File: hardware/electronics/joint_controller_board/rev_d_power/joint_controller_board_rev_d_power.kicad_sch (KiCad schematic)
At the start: 41 parts, among them J1 J_IFACE, J2 J_PWR_IN_RAW, J4 J_PWR_OUT_SW, Q1 BSC016N06NS, Q2 BSC016N06NS, U1 TPS2492PW, U2 LMR36520ADDA, U3 TLV75533PDBV

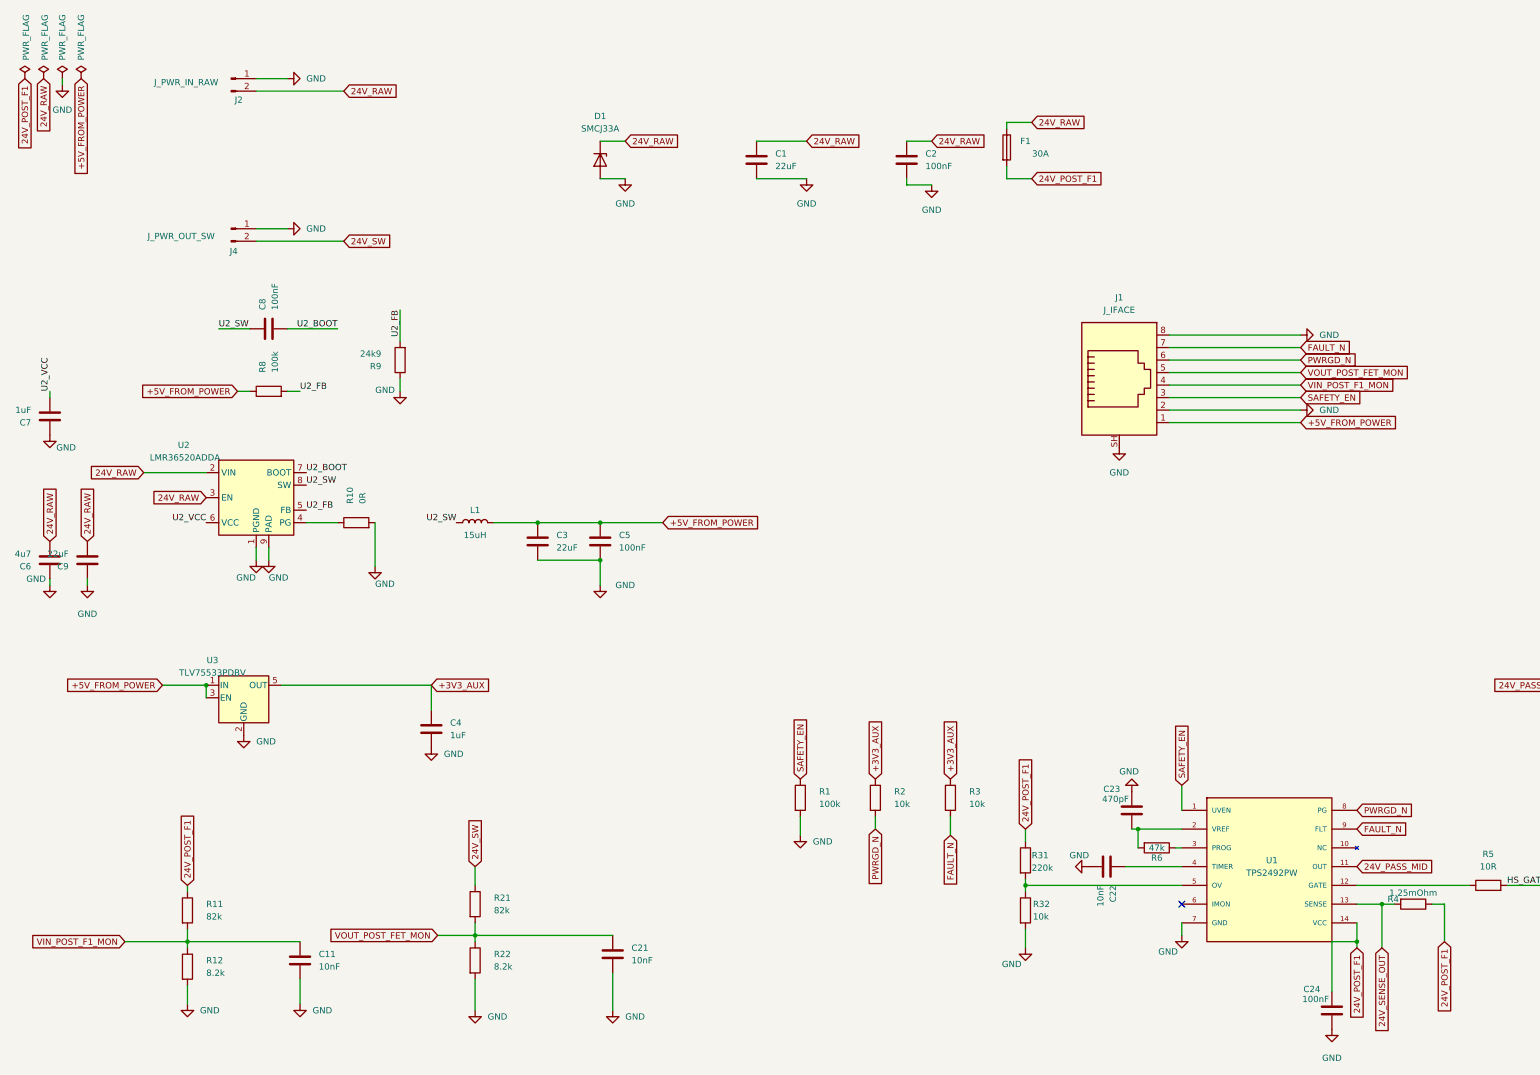
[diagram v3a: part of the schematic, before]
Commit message: feat(rev_d_power): move branch fuse off-board to upstream PDU (Option C1)
Remove on-board F1 fuse + holder from schematic and layout. Per-joint 30A ATO
slow-blow now lives on the upstream PDU / battery distribution board. Saves
~24mm vertical clearance inside joint enclosure (resolved mechanical fit-check
blocker) and protects the full cable run rather than only the PCB. On-board
fast protection preserved via TPS2492 current-limit (~40A latch-off).

Net renames: 24V_POST_F1 -> 24V_RAW (unified), VIN_POST_F1_MON -> VIN_RAW_MON.
RJ45 pin 4 signal name and related schematic descriptions updated accordingly
in ARCHITECTURE.md and COMPONENT_SELECTION.md.

ERC 0/0, DRC 0 violations (2 preexisting XT60 J2/J4 gender-swap warnings
unchanged).

Signed-off-by: graceful-kinematics <info@aliahumanoid.com>
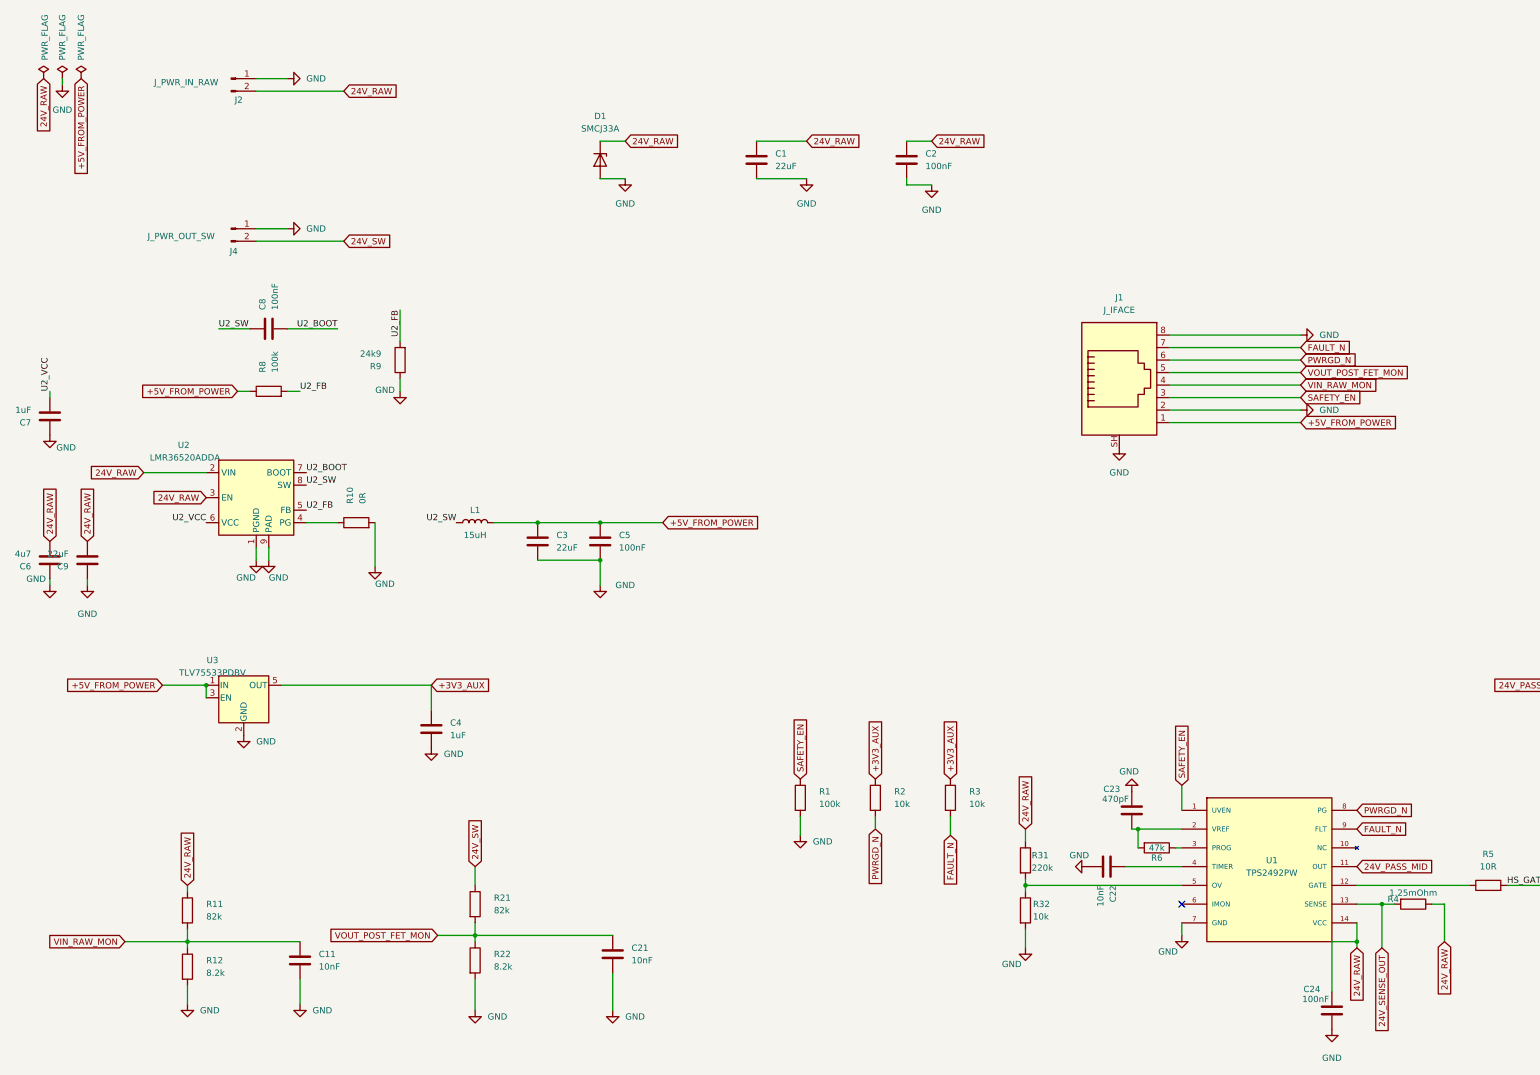
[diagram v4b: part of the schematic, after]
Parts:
- removed F1: 30A, rev_d_power_footprints:FuseHolder_Blade_ATO_Littelfuse_FLR_178.6165, symbol Device:Fuse
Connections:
- net 24V_POST_F1 is gone; now on net 24V_RAW: C24.2, R11.1, R31.1, R4.1, U1.14 (VCC)
- net VIN_POST_F1_MON renamed VIN_RAW_MON

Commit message: feat(rev_d_power): remove raw daisy-chain J3, align XT60 library prefix
Drop the J3 XT60PW-F raw-pass-through connector and its dedicated copper.
The board now has a single raw-input (J2 XT60PW-F) and a single switched
motor output (J4 XT60PW-M). Branch fan-out is handled by the upstream PDU,
consistent with Option C1 external fusing landed in the previous commit.

Also align the J2/J4 footprint library references with the matching
schematic symbols by adding the explicit Connector_AMASS: prefix. Clears
the last two footprint_symbol_mismatch DRC schematic-parity warnings.

Docs updated:
- ARCHITECTURE.md: External Interfaces lists only J_PWR_IN_RAW and
  J_PWR_OUT_SW; Architecture Decision 1 rewritten as "No on-board raw
  daisy-chain output"; power diagram, 6 "Raw daisy-chain sizing" section,
  and test-point list trimmed accordingly; IMON note: pin budget full, not
  routed to RJ45 in this revision.
- COMPONENT_SELECTION.md: topology reflects no raw daisy-chain.
- README.md: board size corrected to 40x60 mm; J2/J4 gender listed; ERC 0/0
  and DRC 0 documented.

ERC 0/0. DRC: 0 violations, 0 unconnected pads, 0 footprint errors.
Board size 40 x 60 mm. BOM 27 rows (was 28 with J3).

Signed-off-by: graceful-kinematics <info@aliahumanoid.com>
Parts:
- J2: footprint Connector_AMASS:AMASS_XT60PW-M_1x02_P7.20mm_Horizontal -> Connector_AMASS:AMASS_XT60PW-F_1x02_P7.20mm_Horizontal; MPN XT60PW-M -> XT60PW-F
- J4: footprint Connector_AMASS:AMASS_XT60PW-F_1x02_P7.20mm_Horizontal -> Connector_AMASS:AMASS_XT60PW-M_1x02_P7.20mm_Horizontal; MPN XT60PW-F -> XT60PW-M
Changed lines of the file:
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@@
 			)
 		)
-		(property "Footprint" "Connector_AMASS:AMASS_XT60PW-M_1x02_P7.20mm_Horizontal"
+		(property "Footprint" "Connector_AMASS:AMASS_XT60PW-F_1x02_P7.20mm_Horizontal"
 			(at 62.23 29.21 0)
 			(effects
@@
 			)
 		)
-		(property "Description" "Raw 24V input XT60"
+		(property "Description" "Raw 24V input XT60 female connector"
 			(at 62.23 29.21 0)
 			(effects
@@
 			)
 		)
-		(property "MPN" "XT60PW-M"
+		(property "MPN" "XT60PW-F"
 			(at 62.23 29.21 0)
 			(effects
@@
 			)
 		)
-		(property "Footprint" "Connector_AMASS:AMASS_XT60PW-F_1x02_P7.20mm_Horizontal"
+		(property "Footprint" "Connector_AMASS:AMASS_XT60PW-M_1x02_P7.20mm_Horizontal"
 			(at 62.23 59.69 0)
 			(effects
@@
 			)
 		)
-		(property "Description" "Switched 24V output XT60"
+		(property "Description" "Switched 24V output XT60 male connector"
 			(at 62.23 59.69 0)
 			(effects
@@
 			)
 		)
-		(property "MPN" "XT60PW-F"
+		(property "MPN" "XT60PW-M"
 			(at 62.23 59.69 0)
 			(effects

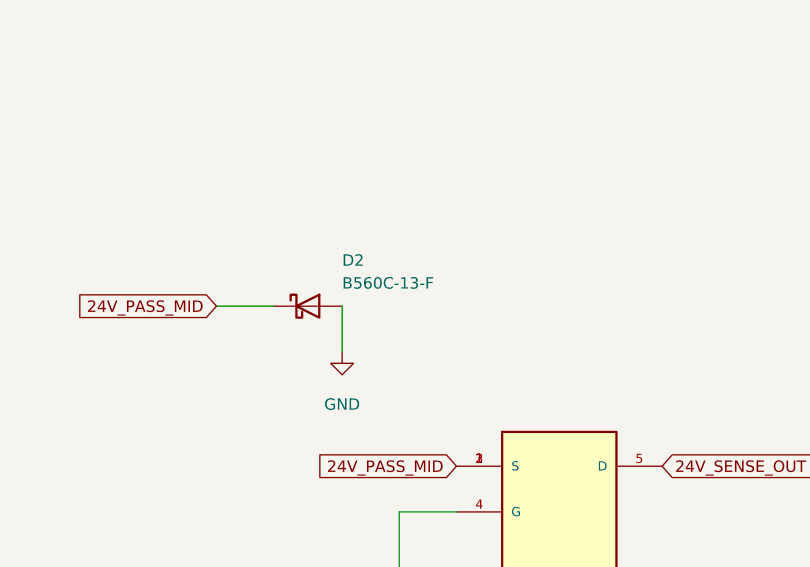
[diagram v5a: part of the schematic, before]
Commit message: fix(rev_d_power): swap D2 to Comchip SS56B-HF after PCBWay BOM review
PCBWay flagged Diodes Inc B560C-13-F in their quotation review: the MPN
is SMC / DO-214AB package while the PCB footprint is D_SMB / DO-214AA.
Swap to Comchip Technology SS56B-HF, a 60V / 5A Schottky in DO-214AA/SMB,
electrically equivalent (V_F, trr, I_F all match). Cathode band polarity
unchanged.

Updated in both schematic and PCB:
- Value / MPN -> SS56B-HF
- Manufacturer -> Comchip Technology
- Datasheet URL -> DigiKey SS56B-HF listing

Footprint D_SMB is preserved. No PCB layout or routing change required.
ERC and DRC remain 0/0.

Signed-off-by: graceful-kinematics <info@aliahumanoid.com>
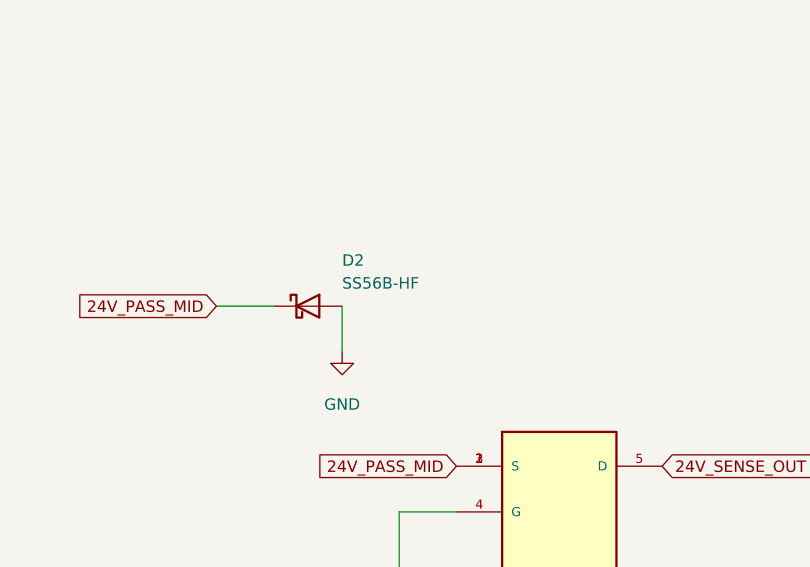
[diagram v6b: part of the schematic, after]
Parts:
- D2: value B560C-13-F -> SS56B-HF; MPN B560C-13-F -> SS56B-HF; Manufacturer Diodes Incorporated -> Comchip Technology
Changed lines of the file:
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@@
 			)
 		)
-		(property "Value" "B560C-13-F"
+		(property "Value" "SS56B-HF"
 			(at 347.98 149.86 0)
 			(effects
@@
 			)
 		)
-		(property "Datasheet" "https://www.diodes.com/assets/Datasheets/ds13005.pdf"
+		(property "Datasheet" "https://www.digikey.com/en/products/detail/comchip-technology/SS56B-HF/11584479"
 			(at 344.17 152.4 0)
 			(effects
@@
 			)
 		)
-		(property "Description" "Negative transient clamp diode from 24V_PASS_MID to GND, 60V 5A Schottky"
+		(property "Description" "Negative transient clamp diode from 24V_PASS_MID to GND, 60V 5A Schottky, SMB/DO-214AA"
 			(at 344.17 152.4 0)
 			(effects
@@
 			)
 		)
-		(property "Manufacturer" "Diodes Incorporated"
+		(property "Manufacturer" "Comchip Technology"
 			(at 344.17 152.4 0)
 			(effects
@@
 			)
 		)
-		(property "MPN" "B560C-13-F"
+		(property "MPN" "SS56B-HF"
 			(at 344.17 152.4 0)
 			(effects

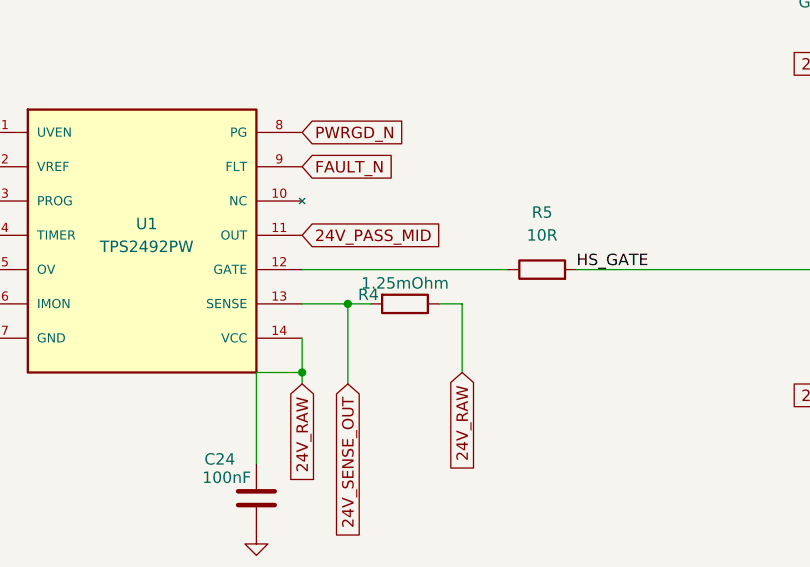
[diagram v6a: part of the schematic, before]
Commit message: hardware(rev_d_power): finalize first-lot CAD — R4 shunt substitution + local XT60 footprint library
PCBWay could not supply the originally specified R4 (WSR21L250FEA, 1.25 mOhm);
the first assembly lot uses the EQ-approved substitution WSR31L500FEA
(1.5 mOhm, 3 W Kelvin), which sets the TPS2492 current limit to Ilim ~= 33.3 A
(vs the ~40 A original design target). Schematic + PCB R4 value/MPN/description
updated accordingly.

Also migrate the J2/J4 XT60 footprints to a board-local library
(rev_d_power_footprints) whose peg-slot geometry matches the already-produced
motor_can_power_hub_rev_a, and un-ignore that library in .gitignore.

ERC 0/0, DRC 0 violations.

Signed-off-by: graceful-kinematics <info@aliahumanoid.com>
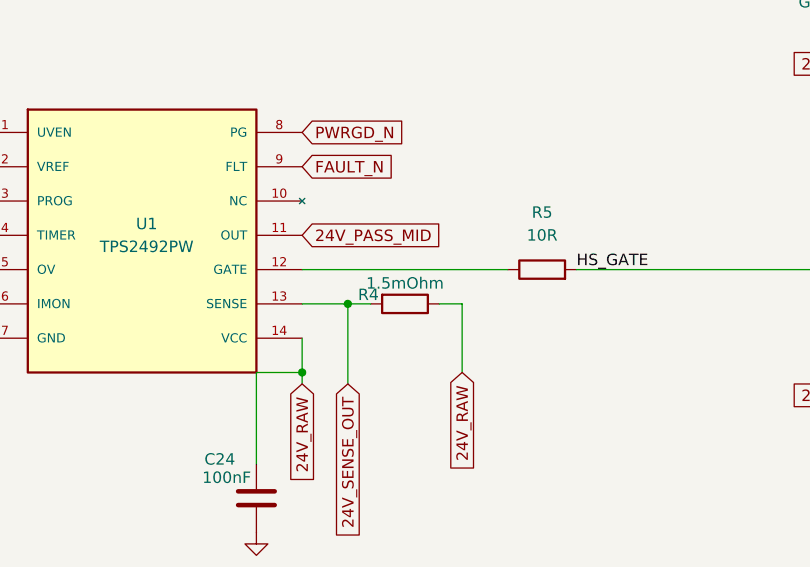
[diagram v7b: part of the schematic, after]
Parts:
- J2: footprint Connector_AMASS:AMASS_XT60PW-F_1x02_P7.20mm_Horizontal -> rev_d_power_footprints:AMASS_XT60PW-F_1x02_P7.20mm_Horizontal
- J4: footprint Connector_AMASS:AMASS_XT60PW-M_1x02_P7.20mm_Horizontal -> rev_d_power_footprints:AMASS_XT60PW-M_1x02_P7.20mm_Horizontal
- R4: value 1.25mOhm -> 1.5mOhm; MPN WSR21L250FEA -> WSR31L500FEA
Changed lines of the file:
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@@
 			)
 		)
-		(property "Footprint" "Connector_AMASS:AMASS_XT60PW-F_1x02_P7.20mm_Horizontal"
+		(property "Footprint" "rev_d_power_footprints:AMASS_XT60PW-F_1x02_P7.20mm_Horizontal"
 			(at 62.23 29.21 0)
 			(effects
@@
 			)
 		)
-		(property "Footprint" "Connector_AMASS:AMASS_XT60PW-M_1x02_P7.20mm_Horizontal"
+		(property "Footprint" "rev_d_power_footprints:AMASS_XT60PW-M_1x02_P7.20mm_Horizontal"
 			(at 62.23 59.69 0)
 			(effects
@@
 			)
 		)
-		(property "Value" "1.25mOhm"
+		(property "Value" "1.5mOhm"
 			(at 302.26 194.564 90)
 			(effects
@@
 			)
 		)
-		(property "Description" "TPS2492 current-sense shunt, 1.25mOhm 1% 2W Kelvin resistor"
+		(property "Description" "TPS2492 current-sense shunt, 1.5mOhm 1% 3W Kelvin resistor; PCBWay-approved R4 substitution for first assembly lot"
 			(at 302.26 196.85 0)
 			(effects
@@
 			)
 		)
-		(property "MPN" "WSR21L250FEA"
+		(property "MPN" "WSR31L500FEA"
 			(at 302.26 196.85 0)
 			(effects
